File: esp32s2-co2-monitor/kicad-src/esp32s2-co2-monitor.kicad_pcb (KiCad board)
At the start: 4 copper layers, 70.3 x 42.8 mm, 98 parts, among them J1 USB_C, J2 Conn_01x10_MountingPin, J3 Conn_01x07_Male, J4 JST, SW1 SW_Push, SW2 SW_Push, SW3 SW_Push, U1 USBLC6-2, U2 TLV62569DRL, U3 ESP32-S2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

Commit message: Update esp32s2 co2 monitor
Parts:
- added C23: 2.2uF, Capacitor_SMD:C_0402_1005Metric, F.Cu at (195.1, 89.5)
- added C24: 22uF, Capacitor_SMD:C_0603_1608Metric, F.Cu at (194.6, 88.2)
- added C25: 4.7uF, Capacitor_SMD:C_0402_1005Metric, F.Cu at (193.4, 83.4)
- added L3: 2.2uH, Inductor_SMD:L_0805_2012Metric, F.Cu at (197.2, 87.0)
- added R18: 36.5k, Resistor_SMD:R_0402_1005Metric, F.Cu at (191.9, 84.8)
- added R19: 16.2k, Resistor_SMD:R_0402_1005Metric, F.Cu at (191.5, 86.3)
- added U7: TPS63900, Package_SON:WSON-10-1EP_2.5x2.5mm_P0.5mm_EP1.2x2mm_ThermalVias, F.Cu at (194.3, 86.0)
- moved R17 38.1 mm to (158.1, 86.3)
- moved TP26 32.5 mm to (163.6, 88.9)
- moved TP28 20.7 mm to (213.1, 93.0)
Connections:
- net no_connect_76 renamed no_connect_81
- C18 pad 1: +3V3 -> +5V
- J2 pad 6: +3V3 -> +5V
- J2 pad 7: +3V3 -> +5V
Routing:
- net /RTC_OUT: track 66.6 -> 125.7 mm
- net /V_SYS: track 14.8 -> 33.6 mm, vias 2 -> 3
- net /LCD_COM: track 33.5 -> 48.4 mm, vias 2 -> 3
- net +5V: track 0.00 -> 12.8 mm, vias 0 -> 1
- net GND: track 81.8 -> 92.6 mm, vias 181 -> 180
- net /CHG_PG: track 36.9 -> 45.5 mm, vias 3 -> 2
- net +3V3: track 21.8 -> 18.5 mm, vias 90 -> 83
- net Net-(L3-Pad2): track 0.00 -> 2.73 mm
- net Net-(L3-Pad1): track 0.00 -> 1.87 mm
- net Net-(R18-Pad2): track 0.00 -> 1.46 mm
- net Net-(R19-Pad2): track 0.00 -> 1.24 mm
- net /CHG_STAT: track 42.8 -> 42.3 mm

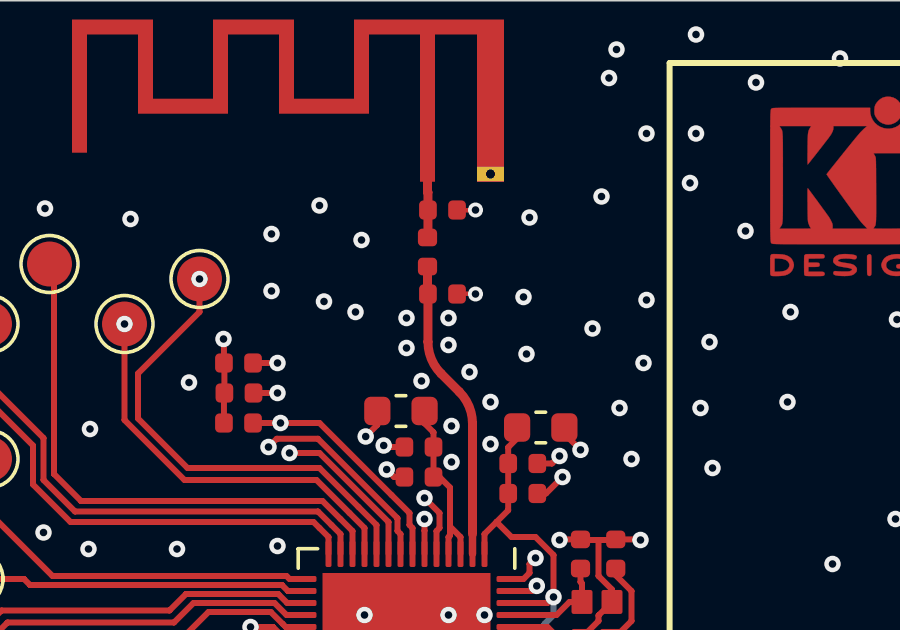
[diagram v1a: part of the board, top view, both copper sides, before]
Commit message: esp32s2-co2-monitor: Update antenna
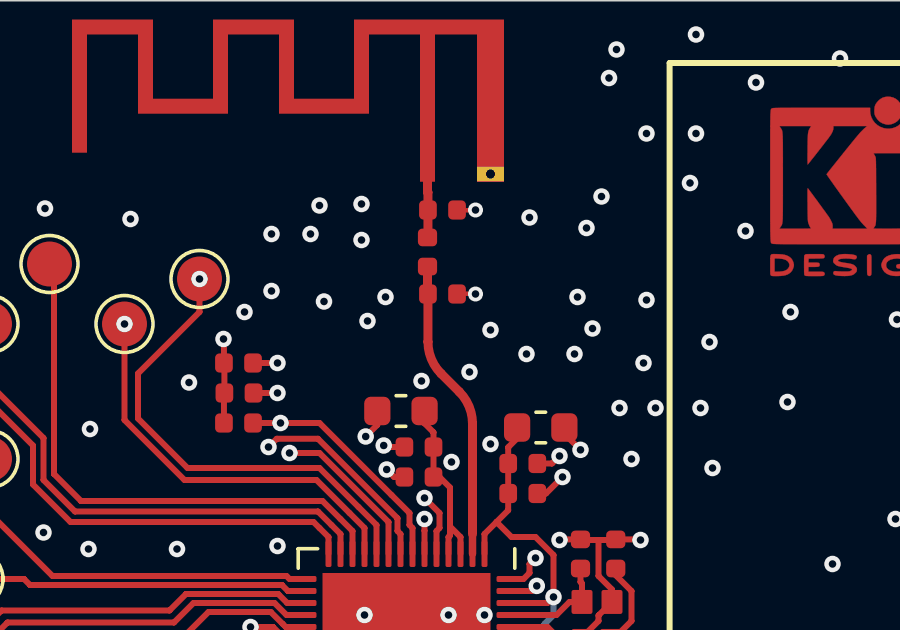
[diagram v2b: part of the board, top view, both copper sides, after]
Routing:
- net GND: vias 180 -> 183
- net +3V3: vias 83 -> 82
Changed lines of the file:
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@@
   (via (at 220.15 56.5) (size 0.55) (drill 0.25) (layers "F.Cu" "B.Cu") (net 1))
   (via (at 211.25 68.5) (size 0.55) (drill 0.25) (layers "F.Cu" "B.Cu") (net 1))
+  (via (at 170.5 63.6) (size 0.55) (drill 0.25) (layers "F.Cu" "B.Cu") (net 1))
   (via (at 206.35 75.85) (size 0.55) (drill 0.25) (layers "F.Cu" "B.Cu") (net 1))
   (via (at 178.2 60.2) (size 0.5) (drill 0.25) (layers "F.Cu" "B.Cu") (net 1))
@@
   (via (at 157.7 87.9) (size 0.55) (drill 0.25) (layers "F.Cu" "B.Cu") (net 1))
   (via (at 218.85 82.6) (size 0.55) (drill 0.25) (layers "F.Cu" "B.Cu") (net 1))
-  (via (at 177.4 67.4) (size 0.55) (drill 0.25) (layers "F.Cu" "B.Cu") (net 1))
   (via (at 205.3 73.6) (size 0.55) (drill 0.25) (layers "F.Cu" "B.Cu") (net 1))
-  (via (at 178.7 66.6) (size 0.55) (drill 0.25) (layers "F.Cu" "B.Cu") (net 1))
+  (via (at 181.5 65) (size 0.55) (drill 0.25) (layers "F.Cu" "B.Cu") (net 1))
   (via (at 184.95 92.95) (size 0.55) (drill 0.25) (layers "F.Cu" "B.Cu") (net 1))
   (via (at 181.7 68.194448) (size 0.55) (drill 0.25) (layers "F.Cu" "B.Cu") (net 1))
@@
   (via (at 178.9 91.9) (size 0.55) (drill 0.25) (layers "F.Cu" "B.Cu") (net 1))
   (via (at 182.9 54.85) (size 0.55) (drill 0.25) (layers "F.Cu" "B.Cu") (net 1))
+  (via (at 181.9 60.8) (size 0.55) (drill 0.25) (layers "F.Cu" "B.Cu") (net 1))
+  (via (at 178.7 64.2) (size 0.55) (drill 0.25) (layers "F.Cu" "B.Cu") (net 1))
   (via (at 185.7 66.8) (size 0.55) (drill 0.25) (layers "F.Cu" "B.Cu") (net 1))
   (via (at 221.05 95.05) (size 0.55) (drill 0.25) (layers "F.Cu" "B.Cu") (net 1))
@@
   (via (at 162.500001 92.999999) (size 0.55) (drill 0.25) (layers "F.Cu" "B.Cu") (net 1))
   (via (at 207.4 79.2) (size 0.55) (drill 0.25) (layers "F.Cu" "B.Cu") (net 1))
+  (via (at 181.6 63.1) (size 0.55) (drill 0.25) (layers "F.Cu" "B.Cu") (net 1))
   (via (at 194.7 94.9) (size 0.55) (drill 0.25) (layers "F.Cu" "B.Cu") (net 1))
   (via (at 158.7 60.9) (size 0.55) (drill 0.25) (layers "F.Cu" "B.Cu") (net 1))
-  (via (at 177.3 64.7) (size 0.55) (drill 0.25) (layers "F.Cu" "B.Cu") (net 1))
   (via (at 219.25 76.25) (size 0.55) (drill 0.25) (layers "F.Cu" "B.Cu") (net 1))
   (via (at 157.9 66.9) (size 0.55) (drill 0.25) (layers "F.Cu" "B.Cu") (net 1))
-  (via (at 177.3 63.8) (size 0.55) (drill 0.25) (layers "F.Cu" "B.Cu") (net 1))
   (via (at 204.85 92.6) (size 0.55) (drill 0.25) (layers "F.Cu" "B.Cu") (net 1))
   (via (at 176.4 65.9) (size 0.55) (drill 0.25) (layers "F.Cu" "B.Cu") (net 1))
@@
   (via (at 167 93.9) (size 0.55) (drill 0.25) (layers "F.Cu" "B.Cu") (net 1))
   (via (at 171.6 71.4) (size 0.55) (drill 0.25) (layers "F.Cu" "B.Cu") (net 1))
-  (via (at 175.9 63.8) (size 0.55) (drill 0.25) (layers "F.Cu" "B.Cu") (net 1))
+  (via (at 175.2 63.1) (size 0.55) (drill 0.25) (layers "F.Cu" "B.Cu") (net 1))
   (via (at 174.539999 67.750001) (size 0.55) (drill 0.25) (layers "F.Cu" "B.Cu") (net 1))
   (via (at 160.1 64.6) (size 0.55) (drill 0.25) (layers "F.Cu" "B.Cu") (net 1))
@@
   (via (at 190.3 86.6) (size 0.55) (drill 0.25) (layers "F.Cu" "B.Cu") (net 1))
   (via (at 175.1 90.2) (size 0.55) (drill 0.25) (layers "F.Cu" "B.Cu") (net 1))
+  (via (at 184.2 66.8) (size 0.55) (drill 0.25) (layers "F.Cu" "B.Cu") (net 1))
   (via (at 177.3 73.7) (size 0.55) (drill 0.25) (layers "F.Cu" "B.Cu") (net 1))
   (via (at 155.1 89.7) (size 0.55) (drill 0.25) (layers "F.Cu" "B.Cu") (net 1))
@@
   (via (at 155.075 59.525) (size 0.55) (drill 0.25) (layers "F.Cu" "B.Cu") (net 1))
   (via (at 181.1 69.1) (size 0.55) (drill 0.25) (layers "F.Cu" "B.Cu") (net 1))
+  (via (at 172.7 61) (size 0.55) (drill 0.25) (layers "F.Cu" "B.Cu") (net 1))
   (via (at 181.1 93.9) (size 0.55) (drill 0.25) (layers "F.Cu" "B.Cu") (net 1))
   (via (at 214.1 59.9) (size 0.55) (drill 0.25) (layers "F.Cu" "B.Cu") (net 1))
@@
   (via (at 186.8 94.6) (size 0.55) (drill 0.25) (layers "F.Cu" "B.Cu") (net 1))
   (via (at 191.8 87.3) (size 0.55) (drill 0.25) (layers "F.Cu" "B.Cu") (net 1))
-  (via (at 175.9 64.8) (size 0.55) (drill 0.25) (layers "F.Cu" "B.Cu") (net 1))
+  (via (at 174.4 60) (size 0.55) (drill 0.25) (layers "F.Cu" "B.Cu") (net 1))
   (via (at 203.4 64) (size 0.55) (drill 0.25) (layers "F.Cu" "B.Cu") (net 1))
   (segment (start 194.7 85.25) (end 194.7 87.2) (width 0.2) (layer "In1.Cu") (net 1))
@@
   (via (at 215.05 68.2) (size 0.55) (drill 0.25) (layers "F.Cu" "B.Cu") (net 3))
   (via (at 185.55 91.1) (size 0.55) (drill 0.25) (layers "F.Cu" "B.Cu") (net 3))
-  (via (at 174.2 63.6) (size 0.55) (drill 0.25) (layers "F.Cu" "B.Cu") (net 3))
+  (via (at 174.6 63.9) (size 0.55) (drill 0.25) (layers "F.Cu" "B.Cu") (net 3))
   (via (at 208.6 85.35) (size 0.55) (drill 0.25) (layers "F.Cu" "B.Cu") (net 3))
   (via (at 168.25 71.5) (size 0.55) (drill 0.25) (layers "F.Cu" "B.Cu") (net 3))
@@
   (via (at 185.35 59.3) (size 0.55) (drill 0.25) (layers "F.Cu" "B.Cu") (net 3))
   (via (at 182.1 64.15) (size 0.55) (drill 0.25) (layers "F.Cu" "B.Cu") (net 3))
-  (via (at 179.8 63.1) (size 0.55) (drill 0.25) (layers "F.Cu" "B.Cu") (net 3))
   (via (at 202 85.05) (size 0.55) (drill 0.25) (layers "F.Cu" "B.Cu") (net 3))
   (via (at 152.5 93.55) (size 0.55) (drill 0.25) (layers "F.Cu" "B.Cu") (net 3))
@@
   (segment (start 192.65 86.5) (end 192.45 86.3) (width 0.2) (layer "F.Cu") (net 79))
   (segment (start 192.45 86.3) (end 191.985 86.3) (width 0.2) (layer "F.Cu") (net 79))
+  (zone (net 0) (net_name "") (layer "F.Cu") (hatch edge 0.508)
+    (connect_pads (clearance 0))
+    (min_thickness 0.254)
+    (keepout (tracks allowed) (vias allowed) (pads allowed ) (copperpour not_allowed) (footprints allowed))
+    (fill (thermal_gap 0.508) (thermal_bridge_width 0.508))
+    (polygon
+      (pts
+        (xy 179.8 62.4)
+        (xy 179.4 64.7)
+        (xy 179.4 66.4)
+        (xy 179.4 70.8)
+        (xy 174 70.8)
+        (xy 174 66.9)
+        (xy 174.5 65.2)
+        (xy 175.2 63.5)
+        (xy 175.2 58.8)
+        (xy 179.8 58.8)
+      )
+    )
+  )
   (zone (net 0) (net_name "") (layers "F.Cu" "In1.Cu" "In2.Cu" "B.Cu") (hatch edge 0.508)
     (connect_pads (clearance 0))
@@
         (xy 158.999999 53.169797)
         (xy 181.387697 53.169797)
-        (xy 181.387696 59.399999)
-        (xy 179.2 59.4)
-        (xy 179.1 58.7)
-        (xy 178.3 58.7)
-        (xy 178.2 59.399999)
-        (xy 158.999999 59.400002)
+        (xy 181.4 58.7)
+        (xy 159 58.7)
       )
     )
